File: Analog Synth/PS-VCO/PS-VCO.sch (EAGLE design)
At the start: 37 parts, among them IC1 TL084D, Q1 BC847BS, T1 2N3904, T2 2N3904

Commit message: PS-VCO creating PCB
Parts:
- added LED1: (no value), eagle-ltspice:LED_ELD260
- added R19: 4.7k, rcl:R-US_R0603
- C8, C9: value 10n -> 100n
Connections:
- removed net N$10: CV.P2, R1.1
- removed net N$13: JP2.1, JP2.2
- removed net N$14: JP2.3, JP2.4
- removed net N$15: JP2.5, JP2.6
- removed net N$17: JP2.7, JP2.8
- removed net N$20: R16.2, R17.2, SQUARE1.P2
- removed net N$23: JP2.10, JP2.9
- new net CV_IN: CV.P2, JP2.10, JP2.9, R1.1
- new net CV_LED: IC1B.-IN, IC1B.OUT, R6.1
- new net SQUARE_OUT: JP2.7, JP2.8, R16.2, R17.2, SQUARE1.P2
- net +12V: now also JP2.1, JP2.2
- net -12V: now also C7.-, C9.2, JP2.5, JP2.6; no longer C7.+, C9.1
- net GND: now also C7.+, C9.1, JP2.3, JP2.4, R19.2; no longer C7.-, C9.2
- net N$11: now also IC1B.+IN; no longer IC1A.+IN
- net N$12: now also LED1.C, R19.1; no longer IC1A.-IN, IC1A.OUT, R6.1
- net N$18: now also LED1.A
- net N$21: now also IC1A.OUT; no longer IC1B.OUT
- net N$22: now also IC1A.-IN; no longer IC1B.-IN
- net N$6: now also IC1A.+IN; no longer IC1B.+IN
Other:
- moved on the sheet: C7, C9, IC1A, IC1B, JP2, R16, R17, SQUARE1

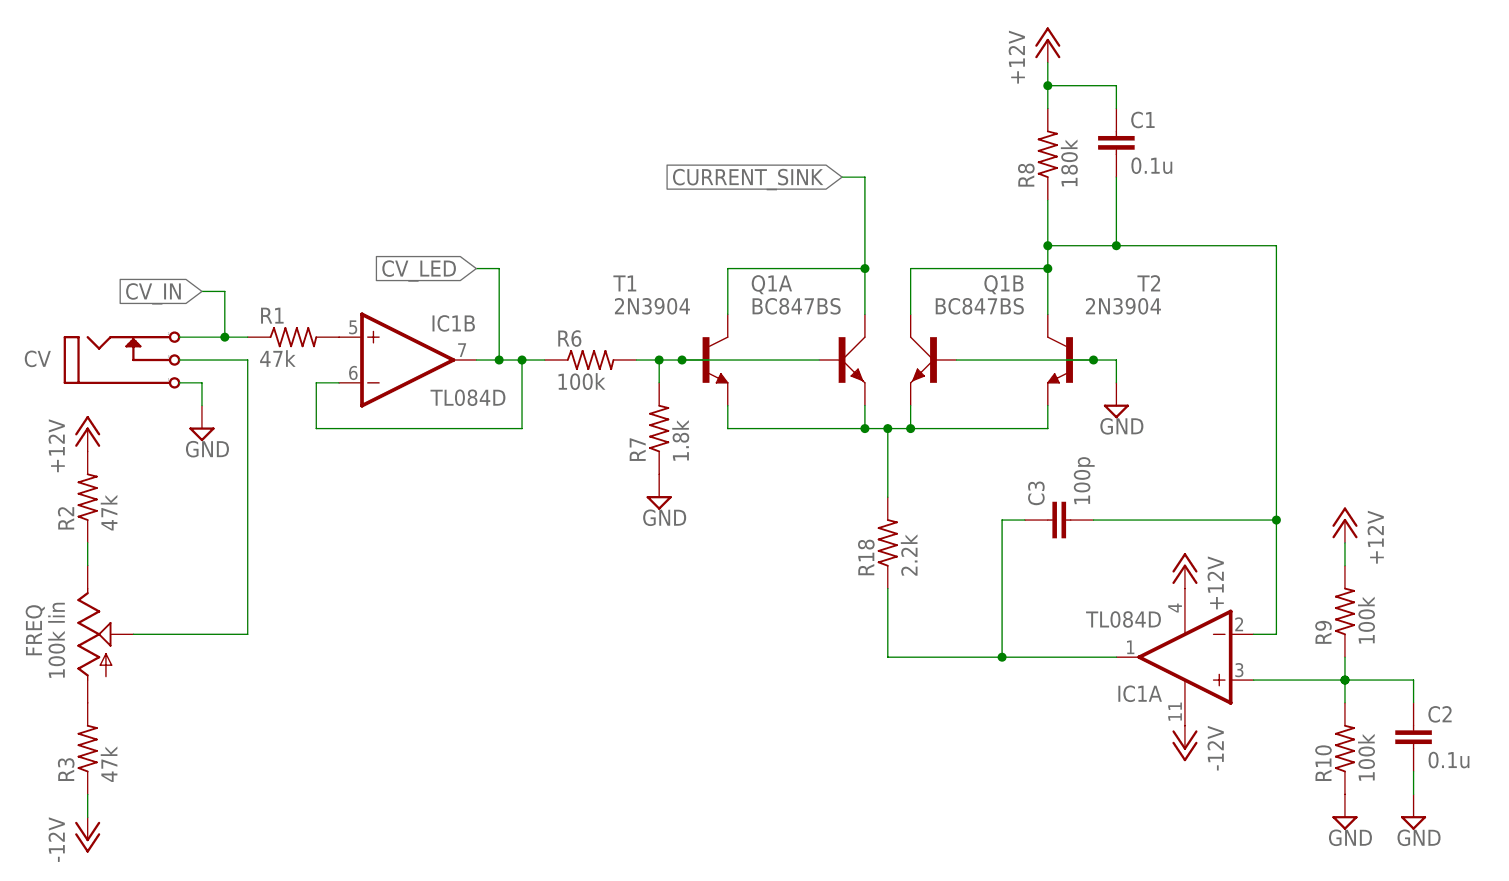
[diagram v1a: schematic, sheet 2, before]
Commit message: PS-VCO added LED - organizing text on PCB
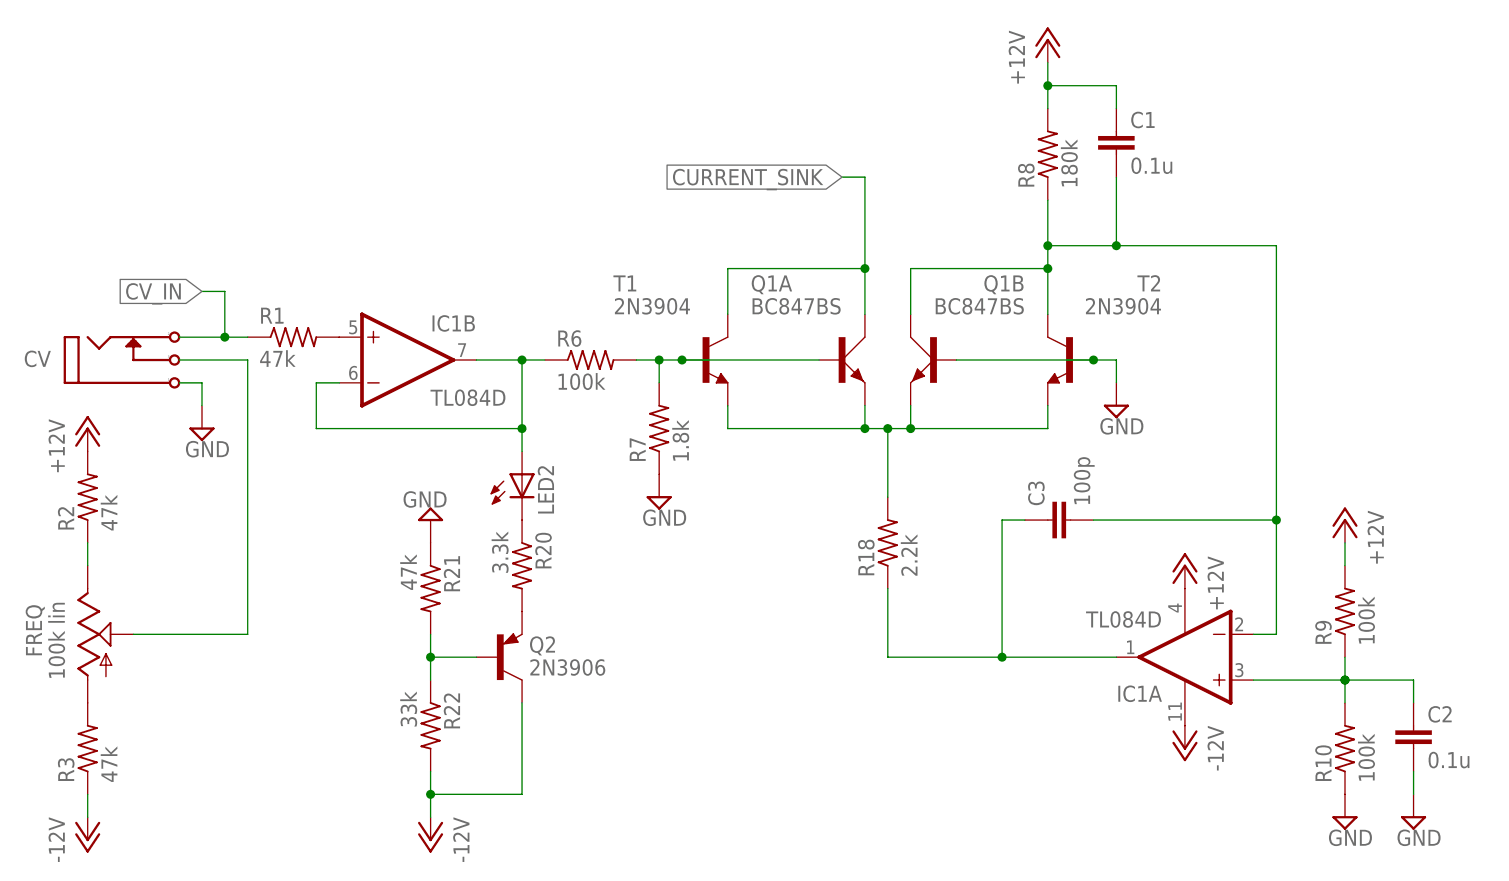
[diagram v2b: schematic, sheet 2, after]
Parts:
- added LED2: (no value), eagle-ltspice:LED_ELD260
- added Q2: 2N3906, transistor-pnp:2N3906
- added R20: 3.3k, rcl:R-US_R0603
- added R21: 47k, rcl:R-US_R0603
- added R22: 33k, rcl:R-US_R0603
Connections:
- new net N$13: Q2.E, R20.2
- new net N$14: LED2.C, R20.1
- new net N$15: Q2.B, R21.2, R22.1
- net -12V: now also Q2.C, R22.2
- net CV_LED: now also LED2.A
- net GND: now also R21.1
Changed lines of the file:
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@@
 <part name="R19" library="rcl" deviceset="R-US_" device="R0603" value="4.7k"/>
 <part name="SUPPLY16" library="supply2" deviceset="GND" device=""/>
+<part name="LED2" library="eagle-ltspice" deviceset="LED_E" device="LD260"/>
+<part name="R20" library="rcl" deviceset="R-US_" device="R0603" value="3.3k"/>
+<part name="Q2" library="transistor-pnp" deviceset="2N3906" device=""/>
+<part name="R21" library="rcl" deviceset="R-US_" device="R0603" value="47k"/>
+<part name="R22" library="rcl" deviceset="R-US_" device="R0603" value="33k"/>
+<part name="SUPPLY17" library="supply2" deviceset="GND" device=""/>
+<part name="P-6" library="supply1" deviceset="-12V" device=""/>
 </parts>
 <sheets>
@@
 <instance part="P+5" gate="1" x="152.4" y="68.58" rot="MR0"/>
 <instance part="R18" gate="G$1" x="101.6" y="66.04" rot="R90"/>
+<instance part="LED2" gate="G$1" x="60.96" y="73.66"/>
+<instance part="R20" gate="G$1" x="60.96" y="63.5" rot="R270"/>
+<instance part="Q2" gate="G$1" x="58.42" y="53.34" smashed="yes">
+<attribute name="NAME" x="61.722" y="53.848" size="1.778" layer="95"/>
+<attribute name="VALUE" x="61.722" y="51.308" size="1.778" layer="96"/>
+</instance>
+<instance part="R21" gate="G$1" x="50.8" y="60.96" rot="R270"/>
+<instance part="R22" gate="G$1" x="50.8" y="45.72" rot="R270"/>
+<instance part="SUPPLY17" gate="GND" x="50.8" y="68.58" rot="R180"/>
+<instance part="P-6" gate="1" x="50.8" y="33.02" rot="MR0"/>
 </instances>
 <busses>
@@
 <wire x1="160.02" y1="40.64" x2="160.02" y2="38.1" width="0.1524" layer="91"/>
 </segment>
+<segment>
+<pinref part="R21" gate="G$1" pin="1"/>
+<pinref part="SUPPLY17" gate="GND" pin="GND"/>
+</segment>
 </net>
 <net name="CV_IN" class="0">
@@
 <wire x1="60.96" y1="78.74" x2="60.96" y2="86.36" width="0.1524" layer="91"/>
 <pinref part="IC1" gate="B" pin="OUT"/>
-<wire x1="60.96" y1="86.36" x2="58.42" y2="86.36" width="0.1524" layer="91"/>
 <pinref part="R6" gate="G$1" pin="1"/>
-<wire x1="58.42" y1="86.36" x2="55.88" y2="86.36" width="0.1524" layer="91"/>
+<wire x1="60.96" y1="86.36" x2="55.88" y2="86.36" width="0.1524" layer="91"/>
 <wire x1="63.5" y1="86.36" x2="60.96" y2="86.36" width="0.1524" layer="91"/>
 <junction x="60.96" y="86.36"/>
-<wire x1="58.42" y1="86.36" x2="58.42" y2="96.52" width="0.1524" layer="91"/>
-<wire x1="58.42" y1="96.52" x2="55.88" y2="96.52" width="0.1524" layer="91"/>
-<label x="55.88" y="96.52" size="1.778" layer="95" rot="R180" xref="yes"/>
-<junction x="58.42" y="86.36"/>
+<pinref part="LED2" gate="G$1" pin="A"/>
+<wire x1="60.96" y1="78.74" x2="60.96" y2="76.2" width="0.1524" layer="91"/>
+<junction x="60.96" y="78.74"/>
 </segment>
 </net>
@@
 <pinref part="IC1" gate="P" pin="V-"/>
 <pinref part="P-3" gate="1" pin="-12V"/>
+</segment>
+<segment>
+<pinref part="R22" gate="G$1" pin="2"/>
+<pinref part="P-6" gate="1" pin="-12V"/>
+<wire x1="50.8" y1="35.56" x2="50.8" y2="38.1" width="0.1524" layer="91"/>
+<pinref part="Q2" gate="G$1" pin="C"/>
+<wire x1="50.8" y1="38.1" x2="50.8" y2="40.64" width="0.1524" layer="91"/>
+<wire x1="60.96" y1="48.26" x2="60.96" y2="38.1" width="0.1524" layer="91"/>
+<wire x1="60.96" y1="38.1" x2="50.8" y2="38.1" width="0.1524" layer="91"/>
+<junction x="50.8" y="38.1"/>
 </segment>
 </net>
@@
 </segment>
 </net>
+<net name="N$14" class="0">
+<segment>
+<pinref part="LED2" gate="G$1" pin="C"/>
+<pinref part="R20" gate="G$1" pin="1"/>
+</segment>
+</net>
+<net name="N$13" class="0">
+<segment>
+<pinref part="R20" gate="G$1" pin="2"/>
+<pinref part="Q2" gate="G$1" pin="E"/>
+</segment>
+</net>
+<net name="N$15" class="0">
+<segment>
+<pinref part="R22" gate="G$1" pin="1"/>
+<pinref part="R21" gate="G$1" pin="2"/>
+<wire x1="50.8" y1="50.8" x2="50.8" y2="53.34" width="0.1524" layer="91"/>
+<wire x1="50.8" y1="55.88" x2="50.8" y2="53.34" width="0.1524" layer="91"/>
+<pinref part="Q2" gate="G$1" pin="B"/>
+<wire x1="50.8" y1="53.34" x2="55.88" y2="53.34" width="0.1524" layer="91"/>
+<junction x="50.8" y="53.34"/>
+</segment>
+</net>

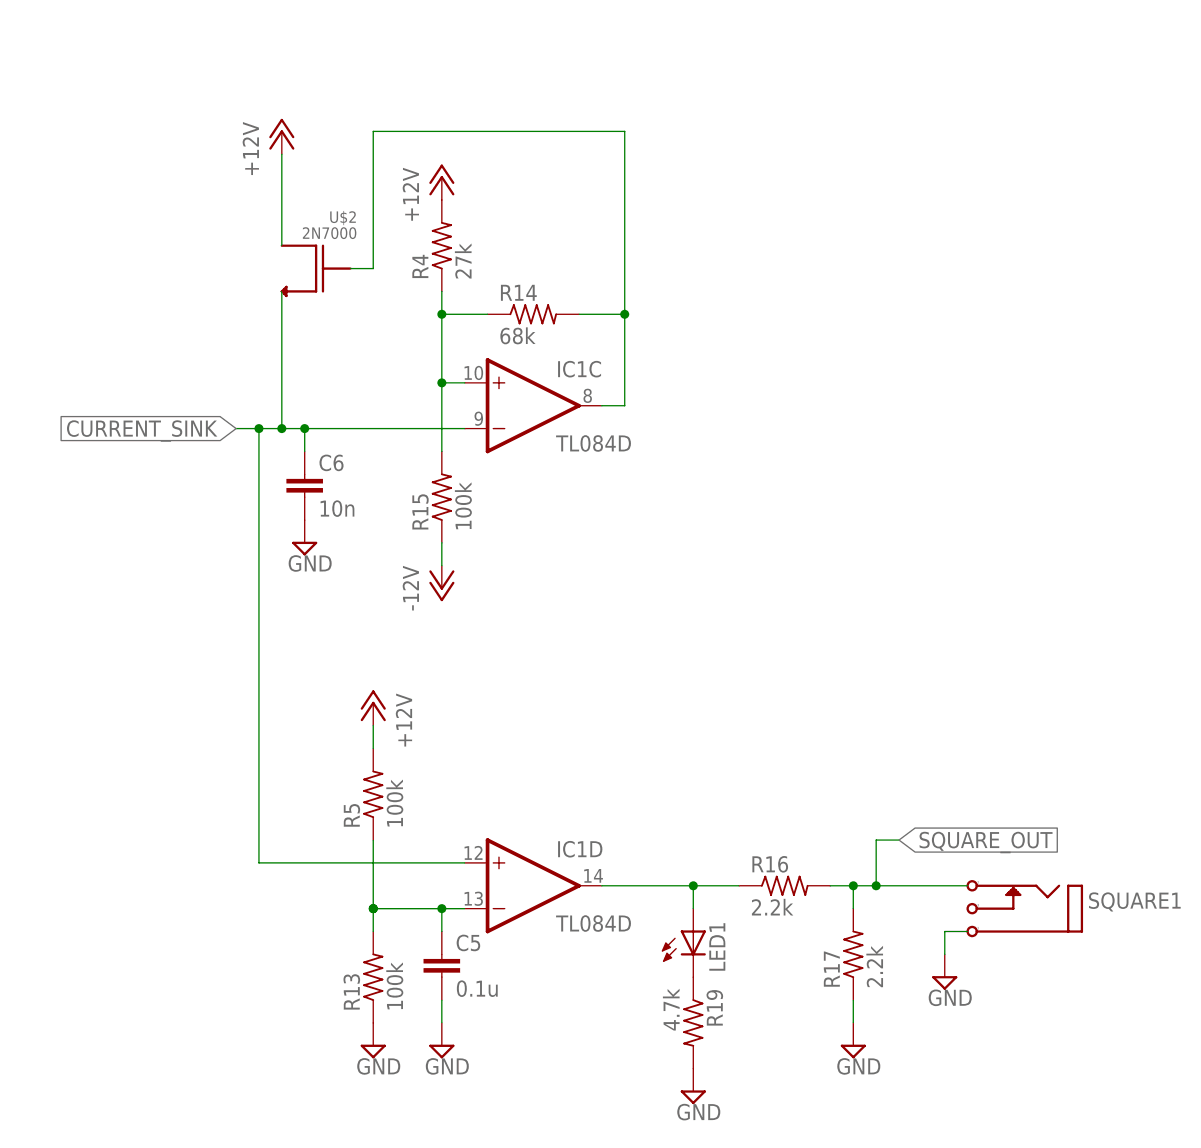
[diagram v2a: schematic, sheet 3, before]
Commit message: PS-VCO updating schematic. made it look cleaner. Added information about theory of operation and instructions for building.
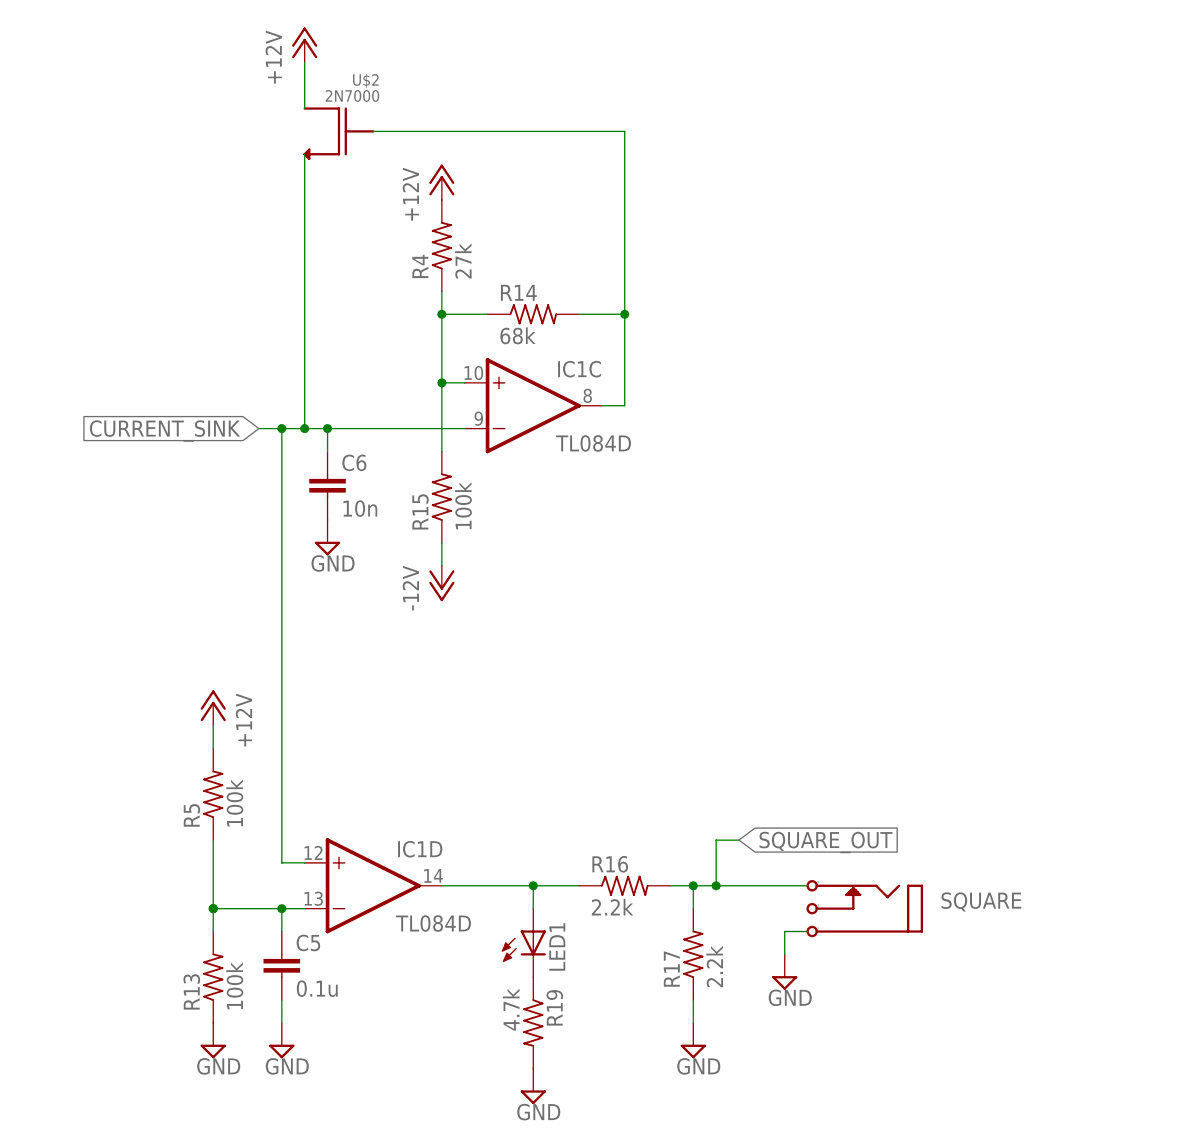
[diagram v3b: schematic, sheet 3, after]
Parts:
- removed SQUARE1: I/O, !synth_sch:MONO_JACK
- added SQUARE: I/O, !synth_sch:MONO_JACK
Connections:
- net GND: now also SQUARE.P$1; no longer SQUARE1.P$1
- net SQUARE_OUT: now also SQUARE.P2; no longer SQUARE1.P2
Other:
- note added: "2015-November"
- note added: "An attempt at creasing minimalistic VCO."
- note added: "Optional LED circuit. Indicates CV level."
- note added: "Optional LED circuit. Indicates Square Wave ON state."
- note added: "PS-VCO"
- note added: "Populate the BC847BS dual pair, OR populate both 2N3904 transistors."
- note added: "Ryan Jensen"
- note added: "This op amp circuit provides hysteresis. It is responsible for switching on the 2N7000 MOSFET when the voltage on C6 reaches some lower threshold. The op amp will use the MOSFET tocharge up the capacitor to some upper threshold voltage , and then switch low, turning off the MOSFET. The voltage waveform developed on C6 is a downward-sloping ramp waveform. (i.e. the voltage decreases linearly over 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"
- moved on the sheet: C5, C6, IC1D, LED1, R13, R16, R17, R19, R5, U$2
